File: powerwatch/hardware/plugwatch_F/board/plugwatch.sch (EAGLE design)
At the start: 124 parts, among them J1 DM3AT-SF-PEJM5, J2 SCREW_TERMNIAL_1, J3 SCREW_TERMNIAL_1, U1 AB1815-T3, U10 OPA369, U11 SIP32510, U12 SIP32510, U13 SIP32510, U14 SIP32510, U2 BGA725L6-ALT, U3 DS2401P+, U4 SAFFB1G56KB0F0A, U5 IRM-03-5V, U6 LIS2DH12, U7 MAX-M8, U8 MAX67XXMAX6749MAX67XX, U9 OPA369, X1 ABS07-32.768KHZ-7-T

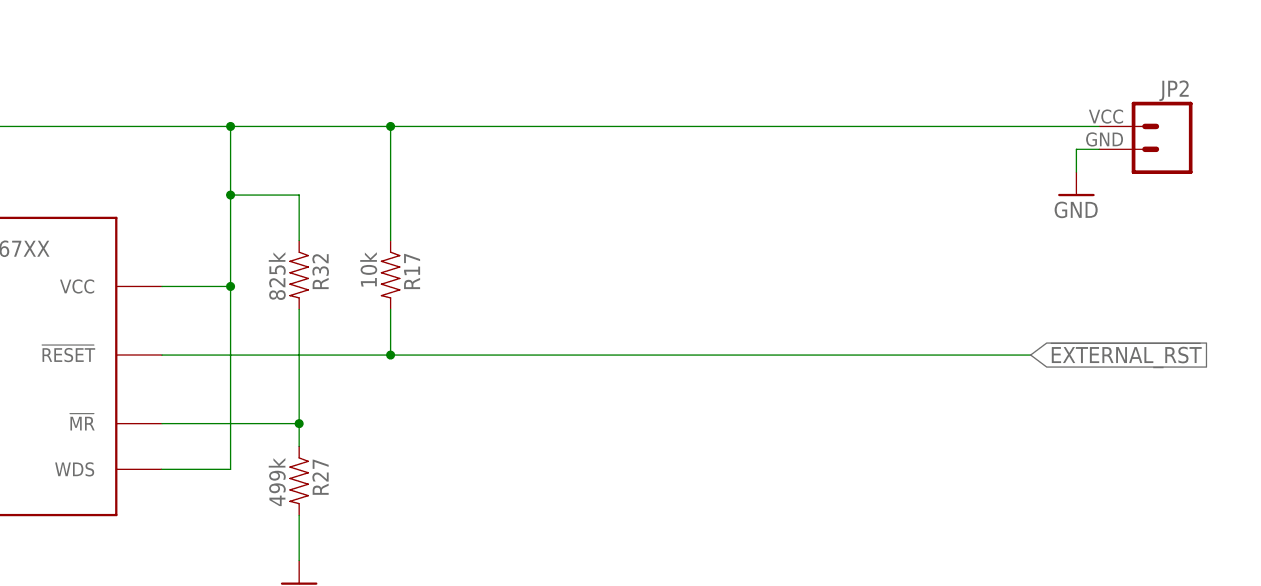
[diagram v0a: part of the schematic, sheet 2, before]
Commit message: add modified board and BOM
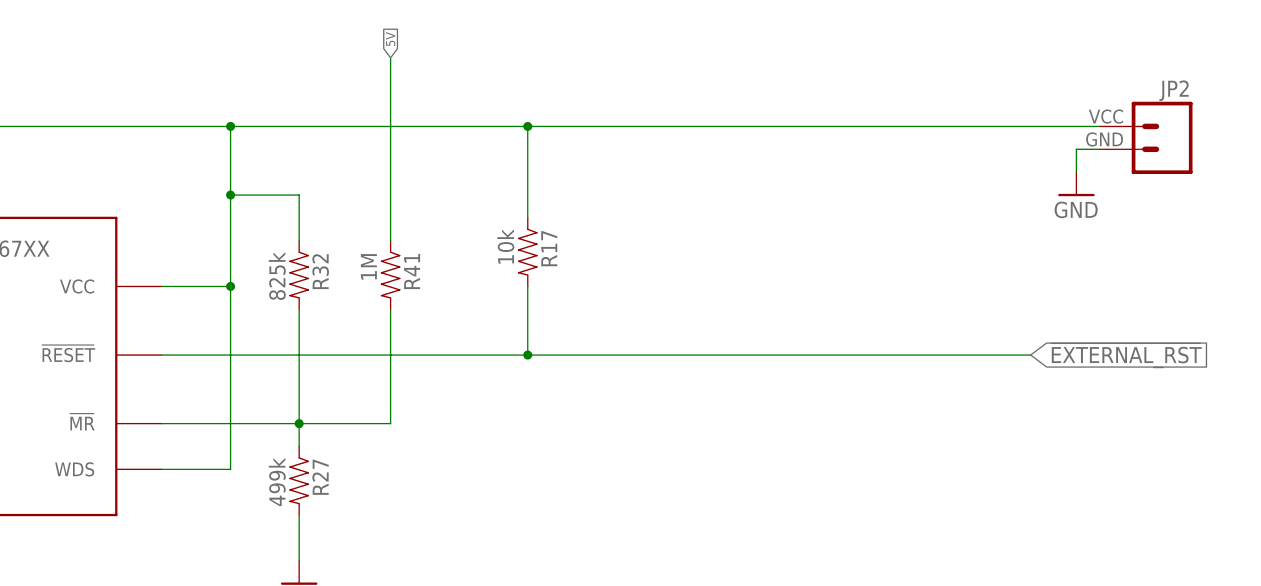
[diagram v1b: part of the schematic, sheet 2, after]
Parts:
- added R41: 1M, passives:RESISTOR0402_RES
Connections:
- net 5V: now also R41.1
- net N$31: now also R41.2
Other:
- moved on the sheet: R17
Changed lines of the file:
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@@
 <?xml version="1.0" encoding="utf-8"?>
 <!DOCTYPE eagle SYSTEM "eagle.dtd">
-<eagle version="9.1.3">
+<eagle version="9.0.1">
 <drawing>
 <settings>
-<setting alwaysvectorfont="no"/>
+<setting alwaysvectorfont="yes"/>
 <setting verticaltext="up"/>
 </settings>
@@
 <part name="U14" library="chips" deviceset="SIP32510" device=""/>
 <part name="SUPPLY11" library="umich" deviceset="GND" device=""/>
+<part name="R41" library="passives" deviceset="RESISTOR" device="0402_RES" value="1M">
+<attribute name="DESCRIPTION" value="RES 1M OHM 1% 1/16W 0402"/>
+<attribute name="DIGIKEY" value="RMCF0402FT1M00CT-ND"/>
+<attribute name="MANUFACTURER" value="Stackpole Electronics Inc."/>
+<attribute name="MPN" value="RMCF0402FT1M00"/>
+</part>
 </parts>
 <sheets>
@@
 <attribute name="DESCRIPTION" x="99.06" y="53.34" size="1.016" layer="96" rot="R270" align="bottom-center" display="off"/>
 </instance>
-<instance part="R17" gate="G$1" x="149.86" y="147.32" rot="R270">
-<attribute name="DIGIKEY" x="149.86" y="147.32" size="1.27" layer="96" rot="R270" display="off"/>
-<attribute name="DESCRIPTION" x="149.86" y="147.32" size="1.016" layer="96" rot="R270" align="bottom-center" display="off"/>
+<instance part="R17" gate="G$1" x="165.1" y="149.86" rot="R270">
+<attribute name="DIGIKEY" x="165.1" y="149.86" size="1.27" layer="96" rot="R270" display="off"/>
+<attribute name="DESCRIPTION" x="165.1" y="149.86" size="1.016" layer="96" rot="R270" align="bottom-center" display="off"/>
 </instance>
 <instance part="JP1" gate="G$1" x="53.34" y="162.56">
@@
 <attribute name="DIGIKEY" x="91.44" y="53.34" size="1.27" layer="96" rot="R270" display="off"/>
 <attribute name="DESCRIPTION" x="91.44" y="53.34" size="1.016" layer="96" rot="R270" align="bottom-center" display="off"/>
+</instance>
+<instance part="R41" gate="G$1" x="149.86" y="147.32" rot="R270">
+<attribute name="DIGIKEY" x="149.86" y="147.32" size="1.27" layer="96" rot="R270" display="off"/>
+<attribute name="MANUFACTURER" x="149.86" y="147.32" size="1.016" layer="96" rot="R180" align="bottom-center" display="off"/>
+<attribute name="MPN" x="149.86" y="147.32" size="1.016" layer="96" rot="R180" align="bottom-center" display="off"/>
+<attribute name="DESCRIPTION" x="149.86" y="147.32" size="1.016" layer="96" rot="R180" align="bottom-center" display="off"/>
 </instance>
 </instances>
@@
 <segment>
 <wire x1="60.96" y1="165.1" x2="132.08" y2="165.1" width="0.1524" layer="91"/>
-<wire x1="132.08" y1="165.1" x2="149.86" y2="165.1" width="0.1524" layer="91"/>
-<wire x1="149.86" y1="165.1" x2="228.6" y2="165.1" width="0.1524" layer="91"/>
+<wire x1="132.08" y1="165.1" x2="165.1" y2="165.1" width="0.1524" layer="91"/>
+<wire x1="165.1" y1="165.1" x2="228.6" y2="165.1" width="0.1524" layer="91"/>
 <pinref part="U8" gate="G$1" pin="VCC"/>
 <wire x1="124.46" y1="147.32" x2="132.08" y2="147.32" width="0.1524" layer="91"/>
@@
 <junction x="132.08" y="147.32"/>
 <pinref part="R17" gate="G$1" pin="1"/>
-<wire x1="149.86" y1="152.4" x2="149.86" y2="165.1" width="0.1524" layer="91"/>
-<junction x="149.86" y="165.1"/>
+<wire x1="165.1" y1="154.94" x2="165.1" y2="165.1" width="0.1524" layer="91"/>
+<junction x="165.1" y="165.1"/>
 <pinref part="JP1" gate="G$1" pin="2"/>
 <pinref part="JP2" gate="G$1" pin="2"/>
@@
 <net name="!EXTERNAL_RST" class="0">
 <segment>
-<wire x1="124.46" y1="139.7" x2="149.86" y2="139.7" width="0.1524" layer="91"/>
+<wire x1="124.46" y1="139.7" x2="165.1" y2="139.7" width="0.1524" layer="91"/>
 <label x="220.98" y="139.7" size="1.778" layer="95" xref="yes"/>
 <pinref part="U8" gate="G$1" pin="!RESET"/>
 <pinref part="R17" gate="G$1" pin="2"/>
-<wire x1="149.86" y1="139.7" x2="220.98" y2="139.7" width="0.1524" layer="91"/>
-<wire x1="149.86" y1="144.78" x2="149.86" y2="139.7" width="0.1524" layer="91"/>
-<junction x="149.86" y="139.7"/>
+<wire x1="165.1" y1="139.7" x2="220.98" y2="139.7" width="0.1524" layer="91"/>
+<wire x1="165.1" y1="147.32" x2="165.1" y2="139.7" width="0.1524" layer="91"/>
+<junction x="165.1" y="139.7"/>
 </segment>
 </net>
@@
 <wire x1="124.46" y1="132.08" x2="139.7" y2="132.08" width="0.1524" layer="91"/>
 <junction x="139.7" y="132.08"/>
+<pinref part="R41" gate="G$1" pin="2"/>
+<wire x1="149.86" y1="144.78" x2="149.86" y2="132.08" width="0.1524" layer="91"/>
+<wire x1="149.86" y1="132.08" x2="139.7" y2="132.08" width="0.1524" layer="91"/>
 </segment>
 </net>
@@
 <label x="190.5" y="99.06" size="1.016" layer="95" rot="R90" xref="yes"/>
 </segment>
-</net>
+<segment>
+<pinref part="R41" gate="G$1" pin="1"/>
+<wire x1="149.86" y1="152.4" x2="149.86" y2="172.72" width="0.1524" layer="91"/>
+<label x="149.86" y="172.72" size="1.016" layer="95" rot="R90" xref="yes"/>
+</segment>
+</net>
